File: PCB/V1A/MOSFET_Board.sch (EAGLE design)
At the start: 274 parts, among them IC301 78L05_TO-220AB-3-BR, IC302 78L05_TO-220AB-3-BR, J301 TEMP, J302 +12V, J303 CTRL, J304 FAN_MOLEX4PIN, J305 FAN_MOLEX4PIN, J306 DUT+, J307 DUT-, Q201 SIRC10DP, Q202 SIRC10DP, Q203 BC817, Q204 BC817, Q205 SIRC10DP, Q206 SIRC10DP, Q207 BC817, Q208 BC807, Q209 BC817, Q210 BC807, Q211 IXTK102N65X2, Q212 IXTK102N65X2, Q301 BC817, Q302 BC817, Q401 BC807, Q402 BC807, Q403 BC807, Q404 BC807, Q405 BC807, Q406 BC807, Q407 BC807, Q408 BC807, Q409 BC807, Q410 BC807, Q411 BC807, Q412 BC807, Q413 BC807, Q414 BC807, U201 AD420, U202 AD420, U203 LT1014I, U204 LT1014I, U205 AD620, U206 AD620, U207 AD620, U208 AD620, U209 LTC1865L, U210 LTC1865L, U301 LP2985-3.1, U302 LP2985-3.1, U303 LP2985-3.1, U304 AD620, U305 LTC1865L, U306 LTC1865L, U307 MAX743, U401 HCPL-063N, U402 HCPL-063N, U403 HCPL-063N, U404 HCPL-063N, U405 HCPL-063N, U406 HCPL-063N, U407 HCPL-063N

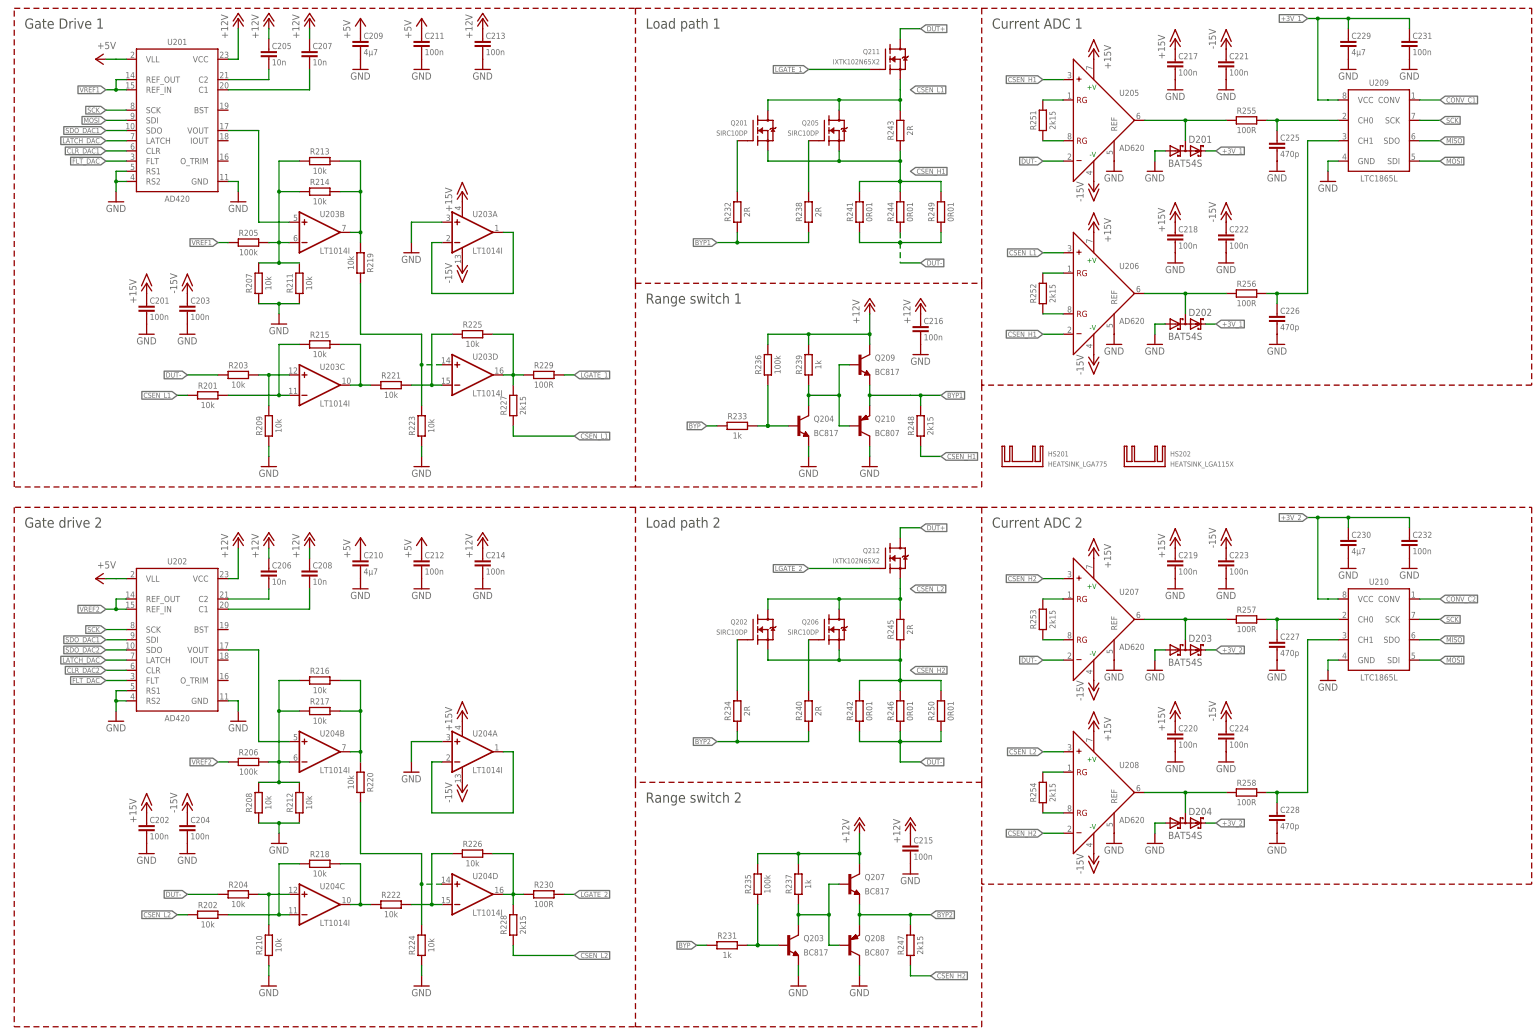
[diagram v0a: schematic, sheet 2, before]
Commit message: Added power amp for load MOSFET gate
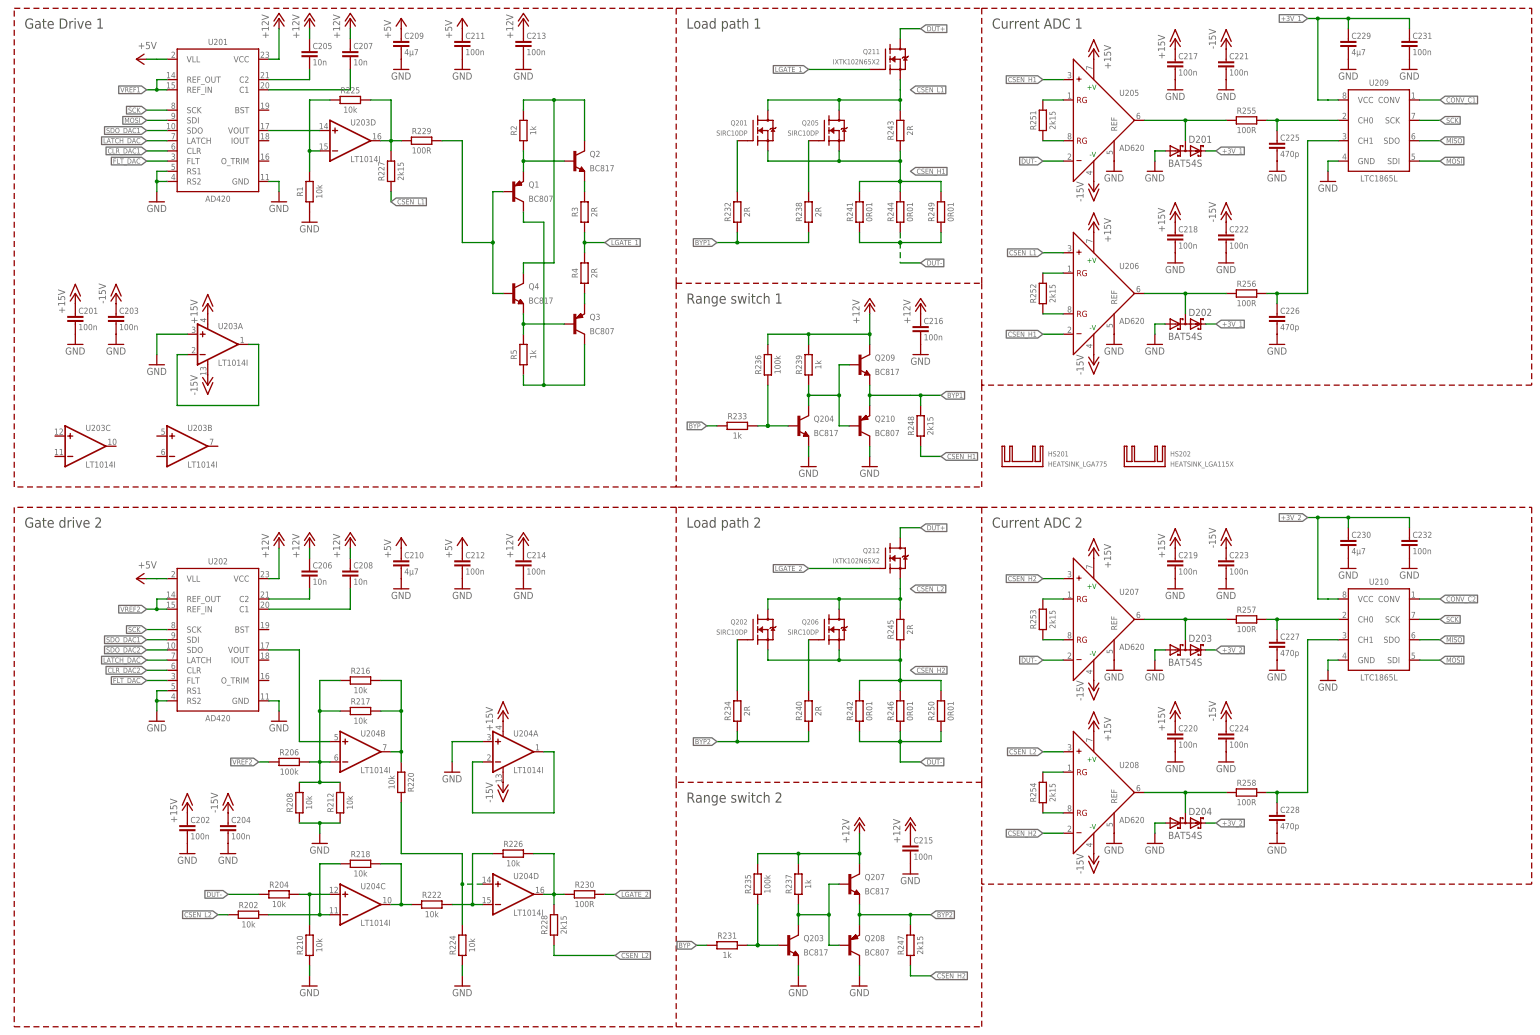
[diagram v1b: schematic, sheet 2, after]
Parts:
- removed R201, R203, R207, R209, R211, R213, R214, R215, R219, R221, R223: 10k, passives:R-EU-1608
- removed R205: 100k, passives:R-EU-1608
- added Q1, Q3: BC807, transistors:BC807
- added Q2, Q4: BC817, transistors:BC817
- added R1: 10k, passives:R-EU-1608
- added R2, R5: 1k, passives:R-EU-1608
- added R3, R4: 2R, passives:R-EU-3216
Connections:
- removed net N$12: R205.2, R207.2, R211.2, R213.1, R214.1, U203B.-IN
- new net N$67: Q1.B, Q4.B, R229.2
- new net N$68: Q3.B, Q4.E, R5.2
- net CSEN_L1: no longer R201.1
- net DAC_VOUT: now also U203D.+IN; no longer U203B.+IN
- net DUT-: no longer R203.1
- net GND: now also R1.1; no longer R207.1, R209.1, R211.1, R223.1
- net LGATE_1: now also R3.1, R4.2; no longer R229.2
- net N$1: now also Q1.E, Q2.B, R2.1; no longer R203.2, R209.2, U203C.+IN
- net N$11: now also Q3.E, R4.1; no longer R213.2, R214.2, R219.1, U203B.OUT
- net N$13: now also Q2.E, R3.2; no longer R215.2, R221.1, U203C.OUT
- net N$14: now also Q2.C, Q4.C, R2.2; no longer R201.2, R215.1, U203C.-IN
- net N$2: now also R1.2; no longer R221.2
- net N$9: now also Q1.C, Q3.C, R5.1; no longer R219.2, R223.2, U203D.+IN
- net VREF1: no longer R205.1
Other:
- moved on the sheet: C201, C202, C203, C204, C205, C206, C207, C208, C209, C210, C211, C212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

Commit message: Changed load path layout
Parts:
- removed C329, C340, C401, C402, C403, C404, C417, C418, C419: 100n, passives:C-EU-1608
- removed C330, C338, C339: 470n, passives:C-EU-1608
- removed C331: 10n, passives:C-EU-2012
- removed C332, C334, C335: 220µ, passives:CPOL_CAPPRD500W60D1000
- removed C333: 10µ, passives:CPOL-6032-C
- removed C337: 470p, passives:C-EU_CAPRR1000W80L1300T400H900
- removed C405, C406, C407, C408, C420, C421, C422: 10n, passives:C-EU-1608
- removed C409, C410, C411, C412, C413, C414, C415, C416, C423, C424, C425, C426, C427, C428: 15p, passives:C-EU-1608
- removed D204, D301: BAT54S, diode:BAT54S
- removed D302, D303: 1N5817-B, diode:1N5817-B
- removed HS201: HEATSINK_LGA775, mechanical:HEATSINK_LGA775
- removed HS202: HEATSINK_LGA115X, mechanical:HEATSINK_LGA115X
- removed IC301, IC302: 78L05_TO-220AB-3-BR, ic:78L05_TO-220AB-3-BR
- removed J301: TEMP, mechanical:HEAD_2X3_MALE
- removed J302: +12V, con-jack:JACK-PLUG1
- removed J303: CTRL, mechanical:HEAD_1X16_MALE
- removed J304, J305: FAN_MOLEX4PIN, mechanical:FAN_MOLEX4PIN
- removed J306: DUT+, mechanical:AMPHENOL_TERM-BLOCK_2
- removed J307: DUT-, mechanical:AMPHENOL_TERM-BLOCK_2
- removed L301, L302: 100µ, passives:L-EU_MSS1260
- removed L303: 4µ7, inductor-coilcraft:MSS7341
- removed MOV301, MOV302: 416NR10D, passives:MOV_9.5-DISK
- removed PS301: RFMM-0505S, modules:RFMM-0505S
- removed Q1, Q208, Q210, Q3, Q401, Q402, Q403, Q404, Q405, Q406, Q407, Q408, Q409, Q410, Q411, Q412, Q413, Q414: BC807, transistors:BC807
- removed Q2, Q203, Q204, Q207, Q209, Q4: BC817, transistors:BC817
- removed Q205, Q206: SIRC10DP, transistors:SIRC10DP
- removed Q211, Q212: IXTK102N65X2, transistors:IXTK102N65X2R
- removed R1, R216, R217, R218, R220, R222, R224, R225, R226: 10k, passives:R-EU-1608
- removed R2, R231, R233, R237, R239, R5: 1k, passives:R-EU-1608
- removed R227, R228, R247, R248, R251, R252, R253, R254: 2k15, passives:R-EU-2012
- removed R229, R230, R255, R256, R257, R258: 100R, passives:R-EU-1608
- removed R232, R234, R238, R240, R243, R245, R3, R4: 2R, passives:R-EU-3216
- removed R235, R236: 100k, passives:R-EU-1608
- removed R241, R242, R244, R246, R249, R250: 0R01, passives:R-EU-6332
- removed R401, R402, R403, R404, R405, R406, R407, R408, R409, R410, R411, R412, R413, R414, R415, R416, R417, R418, R419, R420, R421, R422, R423, R424, R425, R426, R427, R428: 350R, passives:R-EU-1608
- removed SJ301: DUT_GND, jumper:SJW
- removed U210: LTC1865L, ic:LTC1865L
- removed U401, U402, U403, U404, U405, U406, U407: HCPL-063N, ic:HCPL-063N
- added C101, C102, C133, C134: 4µ7, passives:C-EU-3216
- added C103, C104, C105, C106, C111, C112, C113, C114, C119, C120, C121, C122, C123, C124, C125, C126, C127, C128, C135, C136, C239: 100n, passives:C-EU-1608
- added C107, C108, C109, C110: 10n, passives:C-EU-2012
- added C115, C116, C117, C118, C237, C238: 470n, passives:C-EU-1608
- added C129, C130, C131, C132: 470p, passives:C-EU-1608
- added C233: 10µ, passives:CPOL-6032-C
- added C234, C235: 220µ, passives:CPOL_CAPPRD500W60D1000
- added C236: 470p, passives:C-EU_CAPRR1000W80L1300T400H900
- added D101, D102, D103, D104: BAT54S, diode:BAT54S
- added HS101: HEATSINK_LGA775, mechanical:HEATSINK_LGA775
- added HS102: HEATSINK_LGA115X, mechanical:HEATSINK_LGA115X
- added J201: TEMP, mechanical:HEAD_2X3_MALE
- added J202: +12V, con-jack:JACK-PLUG1
- added J203: CTRL, mechanical:HEAD_1X16_MALE
- added J204, J205: FAN_MOLEX4PIN, mechanical:FAN_MOLEX4PIN
- added J206: DUT+, mechanical:AMPHENOL_TERM-BLOCK_2
- added J207: DUT-, mechanical:AMPHENOL_TERM-BLOCK_2
- added L201, L202: 100µ, passives:L-EU_MSS1260
- added L203: 4µ7, inductor-coilcraft:MSS7341
- added MOV201, MOV202: 416NR10D, passives:MOV_9.5-DISK
- added PS201: RFMM-0505S, modules:RFMM-0505S
- added Q101, Q103, Q106, Q108, Q116, Q118, Q303, Q304, Q305, Q306, Q307, Q308, Q309, Q310, Q311, Q312, Q313, Q314: BC807, transistors:BC807
- added Q102, Q104, Q105, Q107, Q111, Q112, Q115, Q117: BC817, transistors:BC817
- added Q109, Q110, Q113, Q114: SIRC10DP, transistors:SIRC10DP
- added Q119, Q120: IXTK102N65X2, transistors:IXTK102N65X2R
- added R101, R102: 49k3, passives:R-EU-1608
- added R103, R104, R105, R106: 5k, passives:R-EU-1608
- added R107, R108, R109, R110, R112, R114, R118, R120, R123, R125: 2R, passives:R-EU-3216
- added R111, R113, R117, R119: 1k, passives:R-EU-1608
- added R115, R116: 100k, passives:R-EU-1608
- added R121, R122, R124, R126, R129, R130: 0R01, passives:R-EU-6332
- added R127, R128, R131, R132, R133, R134, R207: 2k15, passives:R-EU-2012
- added R135, R136, R137, R138, R209: 100R, passives:R-EU-1608
- added R201, R203, R205: 2M, passives:R-EU-3216
- added R211, R311, R314, R315, R316, R317, R318, R319, R320, R321, R322, R323, R324, R325, R326, R327, R328: 350R, passives:R-EU-1608
- added SJ201: DUT_GND, jumper:SJW
- added U101, U102: AD420, ic:AD420RW-24
- added U103, U104, U105, U106, U107, U108: AD620, ic:AD620R-8
- added U109, U110: LTC1865L, ic:LTC1865L
- C201, C202, C203, C217, C224: value 100n -> 4µ7; device passives:C-EU-1608 -> passives:C-EU-3216
- C208: value 10n -> 4µ7; device passives:C-EU-2012 -> passives:C-EU-3216
- C211, C212, C213, C215: value 100n -> 470n
- C218: value 100n -> 470p
- C223: value 100n -> 47µ; device passives:C-EU-1608 -> passives:CPOL-7343-DE
- C225: value 470p -> 4µ7; device passives:C-EU-1608 -> passives:C-EU-3216
- C226: value 470p -> 10n; device passives:C-EU-1608 -> passives:C-EU-2012
- C227: value 470p -> 10µ; device passives:C-EU-1608 -> passives:CPOL-6032-C
- C228, C318: value 470p -> 100n
- C229, C301, C302, C303, C317: value 4µ7 -> 100n; device passives:C-EU-3216 -> passives:C-EU-1608
- C230: value 4µ7 -> 470n; device passives:C-EU-3216 -> passives:C-EU-1608
- C231: value 100n -> 10n; device passives:C-EU-1608 -> passives:C-EU-2012
- C232: value 100n -> 220µ; device passives:C-EU-1608 -> passives:CPOL_CAPPRD500W60D1000
- C305, C306, C307: device passives:C-EU-2012 -> passives:C-EU-1608
- C308: value 4µ7 -> 10n; device passives:C-EU-3216 -> passives:C-EU-1608
- C309, C310, C324, C325: value 4µ7 -> 15p; device passives:C-EU-3216 -> passives:C-EU-1608
- C311, C312, C313, C315: value 470n -> 15p
- C314, C316, C328: value 100n -> 15p
- C320, C321, C322: value 100n -> 10n
- C323: value 47µ -> 15p; device passives:CPOL-7343-DE -> passives:C-EU-1608
- C326: value 10n -> 15p; device passives:C-EU-2012 -> passives:C-EU-1608
- C327: value 10µ -> 15p; device passives:CPOL-6032-C -> passives:C-EU-1608
- D202, D203: value BAT54S -> 1N5817-B; device diode:BAT54S -> diode:1N5817-B
- Q201, Q202: value SIRC10DP -> BC817; device transistors:SIRC10DP -> transistors:BC817
- Q301, Q302: value BC817 -> BC807; device transistors:BC817 -> transistors:BC807
- R202, R208: value 10k -> 2k15; device passives:R-EU-1608 -> passives:R-EU-2012
- R204: value 10k -> 2M; device passives:R-EU-1608 -> passives:R-EU-3216
- R206: value 100k -> 2M; device passives:R-EU-1608 -> passives:R-EU-3216
- R212, R310: value 10k -> 350R
- R301, R303, R304, R305, R306: value 2M -> 350R; device passives:R-EU-3216 -> passives:R-EU-1608
- R302, R307, R308: value 2k15 -> 350R; device passives:R-EU-2012 -> passives:R-EU-1608
- R309: value 100R -> 350R
- U201, U202: value AD420 -> LP2985-3.1; device ic:AD420RW-24 -> ic:LP2985-3.1
- U203: value LT1014I -> LP2985-3.1; device ic:LT1014ISW -> ic:LP2985-3.1
- U204: value LT1014I -> AD620; device ic:LT1014ISW -> ic:AD620R-8
- U205, U206: value AD620 -> 78L05_TO-220AB-3-BR; device ic:AD620R-8 -> ic:78L05_TO-220AB-3-BR
- U207, U208: value AD620 -> LTC1865L; device ic:AD620R-8 -> ic:LTC1865L
- U209: value LTC1865L -> MAX743; device ic:LTC1865L -> ic:MAX743WE
- U301, U302, U303: value LP2985-3.1 -> HCPL-063N; device ic:LP2985-3.1 -> ic:HCPL-063N
- U304: value AD620 -> HCPL-063N; device ic:AD620R-8 -> ic:HCPL-063N
- U305, U306: value LTC1865L -> HCPL-063N; device ic:LTC1865L -> ic:HCPL-063N
- U307: value MAX743 -> HCPL-063N; device ic:MAX743WE -> ic:HCPL-063N
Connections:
- removed net DAC_VOUT: U201.VOUT, U203D.+IN
- removed net DAC_VOUT1: U202.VOUT, U204B.+IN
- removed net N$52: R226.2, R228.2, R230.1, U204D.OUT
- removed net N$53: R220.2, R224.2, U204D.+IN
- removed net N$54: R216.2, R217.2, R220.1, U204B.OUT
- removed net N$55: U204A.-IN, U204A.OUT
- new net N$12: Q103.E, Q107.B, R105.1
- net +12V: now also C105.1, C106.1, C107.1, C108.1, C109.1, C110.1, C119.1, C120.1, C212.1, C232.+, J202.3, J204.+12V, J205.+12V, Q115.C, Q117.C, R115.2, R116.2, R117.2, R119.2, U101.VCC, U102.VCC, U205.VI, U206.VI; no longer C205.1, C206.1, C207.1, C208.1, C214.1, C215.1, C216.1, C312.1, C313.1, C332.+, IC301.VI, IC302.VI, J302.3, J304.+12V, J305.+12V, Q207.C, Q209.C, R235.2, R236.2, R237.2, R239.2, U201.VCC, U202.VCC
- net +15V: now also C111.1, C113.1, C115.1, C117.1, C121.1, C122.1, C123.1, C124.1, C216.1, Q102.C, Q104.C, Q105.C, Q107.C, Q202.E, R103.2, R105.2, U103.+V, U104.+V, U105.+V, U106.+V, U107.+V, U108.+V, U204.+V; no longer C201.1, C202.1, C217.1, C218.1, C219.1, C220.1, C316.1, Q302.E, U203A.V+, U204A.V+, U205.+V, U206.+V, U207.+V, U208.+V, U304.+V
- net +3V3: now also C210.1, R310.2, R311.2, R312.2, R314.2, R315.2, R316.2, R319.2, U203.VOUT; no longer C310.1, R410.2, R411.2, R412.2, R414.2, R415.2, R416.2, R419.2, U303.VOUT
- net +3V_1: now also C133.1, C135.1, C208.1, C217.1, C220.1, D101.C2, D102.C2, U109.VCC, U201.VOUT, U207.VCC; no longer C229.1, C231.1, C308.1, C317.1, C320.1, D201.C2, D202.C2, U209.VCC, U301.VOUT, U305.VCC
- net +3V_2: now also C134.1, C136.1, C209.1, C224.1, C228.1, D103.C2, D104.C2, D201.C2, U110.VCC, U202.VOUT, U208.VCC; no longer C230.1, C232.1, C309.1, C324.1, C328.1, D203.C2, D204.C2, D301.C2, U210.VCC, U302.VOUT, U306.VCC
- net +5V: now also C101.1, C102.1, C103.1, C104.1, C203.1, C204.1, C214.1, C221.1, C222.1, C223.+, C225.1, C229.2, C233.+, C301.1, C302.1, C305.1, C306.1, C307.1, C308.1, C317.1, C318.1, C320.1, J201.3, J201.4, L201.1, L203.2, R309.2, R313.2, R322.2, R323.2, R324.2, R326.2, R327.2, U101.VLL, U102.VLL, U203.ON/OFF, U203.VIN, U205.VO, U206.VO, U209.AV+, U209.V+, U209.V+@1, U209.V+@2, U209.V+@3, U301.VCC, U302.VCC, U303.VCC, U304.VCC, U305.VCC, U306.VCC; no longer C209.1, C210.1, C211.1, C212.1, C314.1, C322.1, C323.+, C325.1, C329.2, C333.+, C401.1, C402.1, C403.1, C404.1, C405.1, C406.1, C407.1, C408.1, C417.1, C418.1, C420.1, C421.1, IC301.VO, IC302.VO, J301.3, J301.4, L301.1, L303.2, R409.2, R413.2, R422.2, R423.2, R424.2, R426.2, R427.2, U201.VLL, U202.VLL, U303.ON/OFF, U303.VIN, U307.AV+, U307.V+, U307.V+@1, U307.V+@2, U307.V+@3, U401.VCC, U402.VCC, U403.VCC, U404.VCC, U405.VCC, U406.VCC
- net +5V_I: now also C236.2, C239.1, C319.1, C322.1, J203.16, PS201.+VO, R301.2, R302.2, R303.2, R304.2, R305.2, R306.2, R307.2, R308.2, R317.2, R318.2, R320.2, R321.2, R325.2, R328.2, U307.VCC; no longer C337.2, C340.1, C419.1, C422.1, J303.16, PS301.+VO, R401.2, R402.2, R403.2, R404.2, R405.2, R406.2, R407.2, R408.2, R417.2, R418.2, R420.2, R421.2, R425.2, R428.2, U407.VCC
- net -15V: now also C112.2, C114.2, C116.2, C118.2, C125.1, C126.1, C127.1, C128.1, C219.1, Q101.C, Q103.C, Q106.C, Q108.C, Q201.E, R104.1, R106.1, U103.-V, U104.-V, U105.-V, U106.-V, U107.-V, U108.-V, U204.-V; no longer C203.1, C204.1, C221.1, C222.1, C223.1, C224.1, C319.1, Q301.E, U203A.V-, U204A.V-, U205.-V, U206.-V, U207.-V, U208.-V, U304.-V
- net BPY1G1: now also Q109.G, R112.2; no longer Q201.G, R232.2
- net BYP: now also C309.1, R111.1, R113.1, R309.1, U301.VO1; no longer C409.1, R231.1, R233.1, R409.1, U401.VO1
- net BYP1: now also Q117.E, Q118.E, R112.1, R118.1, R128.1; no longer Q209.E, Q210.E, R232.1, R238.1, R248.1
- net BYP1G2: now also Q113.G, R118.2; no longer Q205.G, R238.2
- net BYP2: now also Q115.E, Q116.E, R114.1, R120.1, R127.2; no longer Q207.E, Q208.E, R234.1, R240.1, R247.2
- net BYP2G1: now also Q110.G, R114.2; no longer Q202.G, R234.2
- net BYP2G2: now also Q114.G, R120.2; no longer Q206.G, R240.2
- net BYP_I: now also J203.8, Q301.B; no longer J303.8, Q401.B
- net CLR_DAC1: now also C324.1, R324.1, U101.CLR, U306.VO1; no longer C424.1, R424.1, U201.CLR, U406.VO1
- net CLR_DAC1_I: now also J203.6, Q310.B; no longer J303.6, Q410.B
- net CLR_DAC2: now also C313.1, R313.1, U102.CLR, U301.VO2; no longer C413.1, R413.1, U202.CLR, U401.VO2
- net CLR_DAC2_I: now also J203.7, Q305.B; no longer J303.7, Q405.B
- net CONV_C1: now also C315.1, R315.1, U109.CONV, U303.VO2; no longer C415.1, R415.1, U209.CONV, U403.VO2
- net CONV_C1_I: now also J203.9, Q307.B; no longer J303.9, Q407.B
- net CONV_C2: now also C316.1, R316.1, U110.CONV, U304.VO2; no longer C416.1, R416.1, U210.CONV, U404.VO2
- net CONV_C2_I: now also J203.11, Q308.B; no longer J303.11, Q408.B
- net CONV_TEMP: now also C311.1, R311.1, U207.CONV, U303.VO1; no longer C411.1, R411.1, U305.CONV, U403.VO1
- net CONV_TEMP_I: now also J203.10, Q303.B; no longer J303.10, Q403.B
- net CONV_V: now also C312.1, R312.1, U208.CONV, U304.VO1; no longer C412.1, R412.1, U306.CONV, U404.VO1
- net CONV_V_I: now also J203.12, Q304.B; no longer J303.12, Q404.B
- net CSEN_H1: now also Q109.S, Q113.S, R121.2, R123.1, R124.2, R128.2, R129.2, U105.+, U106.-; no longer Q201.S, Q205.S, R241.2, R243.1, R244.2, R248.2, R249.2, U205.+, U206.-
- net CSEN_H2: now also Q110.S, Q114.S, R122.2, R125.1, R126.2, R127.1, R130.2, U107.+, U108.-; no longer Q202.S, Q206.S, R242.2, R245.1, R246.2, R247.1, R250.2, U207.+, U208.-
- net CSEN_L1: now also Q109.D, Q113.D, Q119.S, R123.2, U103.REF, U106.+; no longer Q201.D, Q205.D, Q211.S, R227.1, R243.2, U206.+
- net CSEN_L2: now also Q110.D, Q114.D, Q120.S, R125.2, U104.REF, U108.+; no longer Q202.D, Q206.D, Q212.S, R202.1, R228.1, R245.2, U208.+
- net DUT+: now also J206G$2.1, Q119.D, Q120.D; no longer J306G$2.1, Q211.D, Q212.D
- net DUT-: now also J207G$1.1, R121.1, R122.1, R124.1, R126.1, R129.1, R130.1, SJ201.2, U105.-, U107.-; no longer J307G$1.1, R204.1, R241.1, R242.1, R244.1, R246.1, R249.1, R250.1, SJ301.2, U205.-, U207.-
- net FAN1_PWM: now also C323.1, J204.PWM, R323.1, U305.VO1; no longer C423.1, J304.PWM, R423.1, U405.VO1
- net FAN1_PWM_I: now also J203.14, Q309.B; no longer J303.14, Q409.B
- net FAN1_SIG: now also J204.SIG; no longer J304.SIG
- net FAN2_PWM: now also C326.1, J205.PWM, R326.1, U305.VO2; no longer C426.1, J305.PWM, R426.1, U405.VO2
- net FAN2_PWM_I: now also J203.13, Q312.B; no longer J303.13, Q412.B
- net FAN2_SIG: now also J205.SIG; no longer J305.SIG
- net FLT_DAC: now also Q311.B, U101.FLT, U102.FLT; no longer Q411.B, U201.FLT, U202.FLT
- net FLT_DAC_I: now also C325.1, J203.1, R325.1, U307.VO1; no longer C425.1, J303.1, R425.1, U407.VO1
- net GND: now also C101.2, C102.2, C103.2, C104.2, C105.2, C106.2, C111.2, C112.1, C113.2, C114.1, C115.2, C116.1, C117.2, C118.1, C119.2, C120.2, C121.2, C122.2, C123.2, C124.2, C125.2, C126.2, C127.2, C128.2, C129.2, C130.2, C131.2, C132.2, C133.2, C134.2, C135.2, C136.2, C205.2, C206.2, C207.2, C208.2, C223.-, C226.1, C227.-, C229.1, C232.-, C233.-, C234.-, C235.+, C237.2, C238.2, C323.2, C326.2, C327.2, D101.A1, D102.A1, D103.A1, D104.A1, J201.1, J201.2, J202.1, J204.GND, J205.GND, L202.2, PS201.-VI, Q111.E, Q112.E, Q116.C, Q118.C, Q311.C, Q314.C, R207.1, SJ201.1, U101.GND, U101.RS1, U101.RS2, U102.GND, U102.RS1, U102.RS2, U103.-, U104.-, U105.REF, U106.REF, U107.REF, U108.REF, U109.GND, U110.GND, U203.GND, U204.REF, U205.GND, U206.GND, U207.GND, U208.GND, U209.12/15, U209.AGND, U304.GND, U307.C1, U307.C2; no longer C223.2, C226.2, C227.2, C229.2, C232.2, C319.2, C322.2, C323.-, C325.2, C326.1, C327.-, C328.2, C329.1, C330.2, C331.2, C332.-, C333.-, C334.-, C335.+, C338.2, C339.2, C401.2, C402.2, C403.2, C404.2, C405.2, C406.2, C407.2, C408.2, C409.2, C410.2, C411.2, C412.2, C413.2, C414.2, C415.2, C416.2, C417.2, C418.2, C420.2, C421.2, C423.2, C424.2, C426.2, C427.2, D202.A1, D203.A1, D204.A1, D301.A1, IC301.GND, IC302.GND, J301.1, J301.2, J302.1, J304.GND, J305.GND, L302.2, PS301.-VI, Q203.E, Q204.E, Q208.C, Q210.C, Q411.C, Q414.C, R1.1, R208.1, R212.1, R224.1, R307.1, R310.1, SJ301.1, U201.RS1, U201.RS2, U202.RS1, U202.RS2, U203A.+IN, U204A.+IN, U205.REF, U206.REF, U207.REF, U208.REF, U210.GND, U304.REF, U307.12/15, U307.AGND, U307.GND, U401.GND, U402.GND, U403.GND, U404.GND, U405.GND, U406.GND, U407.C1, U407.C2
- net GNDI: now also C239.2, C319.2, C322.2, C325.2, C328.2, J203.15, PS201.-VO, Q301.C, Q302.C, Q303.C, Q304.C, Q305.C, Q306.C, Q307.C, Q308.C, Q309.C, Q310.C, Q312.C, Q313.C, U301.C1, U301.C2, U302.C1, U302.C2, U303.C1, U303.C2, U304.C1, U304.C2, U305.C1, U305.C2, U306.C1, U306.C2, U307.GND; no longer C340.2, C419.2, C422.2, C425.2, C428.2, J303.15, PS301.-VO, Q401.C, Q402.C, Q403.C, Q404.C, Q405.C, Q406.C, Q407.C, Q408.C, Q409.C, Q410.C, Q412.C, Q413.C, U401.C1, U401.C2, U402.C1, U402.C2, U403.C1, U403.C2, U404.C1, U404.C2, U405.C1, U405.C2, U406.C1, U406.C2, U407.GND
- net HIGHC1: now also C129.1, R135.2, U109.CH0; no longer C225.1, R255.2, U209.CH0
- net HIGHC2: now also C131.1, R137.2, U110.CH0; no longer C227.1, R257.2, U210.CH0
- net LATCH_DAC: now also C327.1, R327.1, U101.LATCH, U102.LATCH, U306.VO2; no longer C427.1, R427.1, U201.LATCH, U202.LATCH, U406.VO2
- net LATCH_DAC_I: now also J203.5, Q313.B; no longer J303.5, Q413.B
- net LGATE_1: now also Q119.G, R107.1, R108.2; no longer Q211.G, R3.1, R4.2
- net LGATE_2: now also Q120.G, R109.1, R110.2; no longer Q212.G, R230.2
- net LOWC1: now also C130.1, R136.2, U109.CH1; no longer C226.1, R256.2, U209.CH1
- net LOWC2: now also C132.1, R138.2, U110.CH1; no longer C228.1, R258.2, U210.CH1
- net MISO: now also Q314.B, U109.SDO, U110.SDO, U207.SDO, U208.SDO; no longer Q414.B, U209.SDO, U210.SDO, U305.SDO, U306.SDO
- net MISO_I: now also C328.1, J203.2, R328.1, U307.VO2; no longer C428.1, J303.2, R428.1, U407.VO2
- net MOSI: now also C310.1, R310.1, U101.SDI, U109.SDI, U110.SDI, U207.SDI, U208.SDI, U302.VO1; no longer C410.1, R410.1, U201.SDI, U209.SDI, U210.SDI, U305.SDI, U306.SDI, U402.VO1
- net MOSI_I: now also J203.4, Q302.B; no longer J303.4, Q402.B
- net N$1: now also Q101.E, Q105.B, R103.1; no longer Q1.E, Q2.B, R2.1
- net N$10: now also C205.1, U201.BYP; no longer C305.1, U301.BYP
- net N$11: now also Q106.E, R108.1; no longer Q3.E, R4.1
- net N$13: now also Q105.E, R107.2; no longer Q2.E, R3.2
- net N$14: now also Q108.E, R110.1; no longer Q2.C, Q4.C, R2.2
- net N$15: now also Q107.E, R109.2; no longer U203A.-IN, U203A.OUT
- net N$16: now also D102.C1A2, R136.1, U106.OUT; no longer D202.C1A2, R256.1, U206.OUT
- net N$17: now also Q311.E, R319.1, U307.A1; no longer Q411.E, R419.1, U407.A1
- net N$18: now also Q314.E, R322.1, U307.A2; no longer Q414.E, R422.1, U407.A2
- net N$19: now also Q304.E, R304.1, U304.A1; no longer Q404.E, R404.1, U404.A1
- net N$2: now also R101.2, U103.RG@1; no longer R1.2, R225.1, U203D.-IN
- net N$20: now also Q308.E, R308.1, U304.A2; no longer Q408.E, R408.1, U404.A2
- net N$21: now also Q302.E, R302.1, U302.A1; no longer Q402.E, R402.1, U402.A1
- net N$22: now also Q306.E, R306.1, U302.A2; no longer Q406.E, R406.1, U402.A2
- net N$23: now also R209.1, U204.OUT; no longer R309.1, U304.OUT
- net N$24: now also R205.1, R206.2; no longer R305.1, R306.2
- net N$25: now also Q111.C, Q115.B, Q116.B, R117.1; no longer Q203.C, Q207.B, Q208.B, R237.1
- net N$26: now also R203.2, R205.2; no longer R303.2, R305.2
- net N$27: now also R203.1, R204.2; no longer R303.1, R304.2
- net N$28: now also MOV201.2, MOV202.1; no longer MOV301.2, MOV302.1
- net N$29: now also R206.1, R207.2, U204.+; no longer R306.1, R307.2, U304.+
- net N$3: now also C107.2, U101.C2; no longer C205.2, U201.C2
- net N$30: now also C218.1, D201.C1A2, R209.2, U208.CH0; no longer C318.1, D301.C1A2, R309.2, U306.CH0
- net N$31: now also Q111.B, R111.2, R115.1; no longer Q203.B, R231.2, R235.1
- net N$32: now also C234.+, D202.C, Q202.C, R211.1, U209.FB+; no longer C334.+, D302.C, Q302.C, R312.1, U307.FB+
- net N$33: now also R201.2, R204.1; no longer R301.2, R304.1
- net N$34: now also C231.1, U209.CC-; no longer C331.1, U307.CC-
- net N$35: now also C230.1, U209.SS; no longer C330.1, U307.SS
- net N$36: now also R202.2, U204.-; no longer R302.2, U304.-
- net N$37: now also C226.2, U209.CC+; no longer C326.2, U307.CC+
- net N$38: now also D202.A, L201.2, U209.LX+; no longer D302.A, L301.2, U307.LX+
- net N$39: now also D203.C, L202.1, U209.LX-; no longer D303.C, L302.1, U307.LX-
- net N$4: now also C109.2, U101.C1; no longer C207.2, U201.C1
- net N$40: now also Q309.E, R317.1, U305.A1; no longer Q409.E, R417.1, U405.A1
- net N$41: now also C108.2, U102.C2; no longer C206.2, U202.C2
- net N$42: now also C110.2, U102.C1; no longer C208.2, U202.C1
- net N$43: now also Q103.B, Q104.B, U104.OUT; no longer R206.2, R208.2, R212.2, R216.1, R217.1, U204B.-IN
- net N$44: now also Q104.E, Q108.B, R106.2; no longer R218.2, R222.1, U204C.OUT
- net N$45: now also R210.2, U208.CH1; no longer R310.2, U306.CH1
- net N$46: now also Q312.E, R320.1, U305.A2; no longer Q412.E, R420.1, U405.A2
- net N$47: now also Q301.E, R301.1, U301.A1; no longer Q401.E, R401.1, U401.A1
- net N$48: now also Q305.E, R305.1, U301.A2; no longer Q405.E, R405.1, U401.A2
- net N$49: now also R102.2, U104.RG@1; no longer R202.2, R218.1, U204C.-IN
- net N$5: now also Q112.C, Q117.B, Q118.B, R119.1; no longer Q204.C, Q209.B, Q210.B, R239.1
- net N$50: now also R102.1, U104.RG@2; no longer R204.2, R210.2, U204C.+IN
- net N$51: now also U102.VOUT, U104.+; no longer R222.2, R226.1, U204D.-IN
- net N$56: now also D103.C1A2, R137.1, U107.OUT; no longer D203.C1A2, R257.1, U207.OUT
- net N$57: now also D104.C1A2, R138.1, U108.OUT; no longer D204.C1A2, R258.1, U208.OUT
- net N$58: now also Q310.E, R318.1, U306.A1; no longer Q410.E, R418.1, U406.A1
- net N$59: now also Q313.E, R321.1, U306.A2; no longer Q413.E, R421.1, U406.A2
- net N$6: now also R101.1, U103.RG@2; no longer R225.2, R227.2, R229.1, U203D.OUT
- net N$60: now also C236.1, L203.1, PS201.+VI; no longer C337.1, L303.1, PS301.+VI
- net N$62: now also C206.1, U202.BYP; no longer C306.1, U302.BYP
- net N$63: now also C238.1, Q202.B, R211.2; no longer C339.1, Q302.B, R312.2
- net N$64: now also C235.-, D203.A, Q201.C, R212.1, U209.FB-; no longer C335.-, D303.A, Q301.C, R313.1, U307.FB-
- net N$65: now also C237.1, Q201.B, R212.2; no longer C338.1, Q301.B, R313.2
- net N$66: now also C207.1, U203.BYP; no longer C307.1, U303.BYP
- net N$67: now also Q101.B, Q102.B, U103.OUT; no longer Q1.B, Q4.B, R229.2
- net N$68: now also Q102.E, Q106.B, R104.2; no longer Q3.B, Q4.E, R5.2
- net N$7: now also D101.C1A2, R135.1, U105.OUT; no longer D201.C1A2, R255.1, U205.OUT
- net N$76: now also Q303.E, R303.1, U303.A1; no longer Q403.E, R403.1, U403.A1
- net N$77: now also Q307.E, R307.1, U303.A2; no longer Q407.E, R407.1, U403.A2
- net N$8: now also Q112.B, R113.2, R116.1; no longer Q204.B, R233.2, R236.1
- net N$9: now also U101.VOUT, U103.+; no longer Q1.C, Q3.C, R5.1
- net RG1_H6: now also R208.2, U204.RG@1; no longer R308.2, U304.RG@1
- net RG1_L1: now also R133.2, U107.RG@1; no longer R253.2, U207.RG@1
- net RG1_L2: now also R134.2, U108.RG@1; no longer R254.2, U208.RG@1
- net RG1_L3: now also R131.2, U105.RG@1; no longer R251.2, U205.RG@1
- net RG1_L4: now also R132.2, U106.RG@1; no longer R252.2, U206.RG@1
- net RG2_H6: now also R208.1, U204.RG@2; no longer R308.1, U304.RG@2
- net RG2_L1: now also R133.1, U107.RG@2; no longer R253.1, U207.RG@2
- net RG2_L2: now also R134.1, U108.RG@2; no longer R254.1, U208.RG@2
- net RG2_L3: now also R131.1, U105.RG@2; no longer R251.1, U205.RG@2
- net RG2_L4: now also R132.1, U106.RG@2; no longer R252.1, U206.RG@2
- net SCK: now also C314.1, R314.1, U101.SCK, U102.SCK, U109.SCK, U110.SCK, U207.SCK, U208.SCK, U302.VO2; no longer C414.1, R414.1, U201.SCK, U202.SCK, U209.SCK, U210.SCK, U305.SCK, U306.SCK, U402.VO2
- net SCK_I: now also J203.3, Q306.B; no longer J303.3, Q406.B
- net SDO_DAC1: now also U101.SDO, U102.SDI; no longer U201.SDO, U202.SDI
- net SDO_DAC2: now also U102.SDO; no longer U202.SDO
- net TEMP1: now also C211.1, J201.5, U207.CH0; no longer C311.1, J301.5, U305.CH0
- net TEMP2: now also C215.1, J201.6, U207.CH1; no longer C315.1, J301.6, U305.CH1
- net VREF1: now also C201.1, U101.REF_IN, U101.REF_OUT, U201.ON/OFF, U201.VIN; no longer C301.1, U201.REF_IN, U201.REF_OUT, U301.ON/OFF, U301.VIN
- net VREF2: now also C202.1, U102.REF_IN, U102.REF_OUT, U202.ON/OFF, U202.VIN; no longer C302.1, R206.1, U202.REF_IN, U202.REF_OUT, U302.ON/OFF, U302.VIN
- net VREF_MAX743: now also C227.+, U209.VREF; no longer C327.+, U307.VREF
- net VSENSE+: now also J206G$1.1, MOV201.1, R201.1; no longer J306G$1.1, MOV301.1, R301.1
- net VSENSE-: now also J207G$2.1, MOV202.2, R202.1; no longer J307G$2.1, MOV302.2, R302.1
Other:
- note removed: "+12V"
- note removed: "+12VDC"
- note removed: "+15V"
- note removed: "+15VDC"
- note removed: "+3VDC"
- note removed: "+5V"
- note removed: "+5VDC"
- note removed: "-15V"
- note removed: "-15VDC"
- note removed: "0R002"
- note removed: "2R"
- note removed: "5VDC<-5VDC"
- note removed: "7805"
- note removed: "DAC"
- note removed: "DUT"
- note removed: "Gate Drive"
- note removed: "I/O"
- note removed: "LDO"
- note removed: "MAX743"
- note removed: "MOSFET"
- note removed: "Optocouplers"
- note removed: "Range Switch"
- note removed: "TODO: block diagram"
- note removed: "Vout"
- note removed: "Vref"

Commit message: Cleaned up schematic; PCB layout
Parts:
- added R1: 1k, passives:R-EU-1608
- R310, R311, R312, R314, R315, R316: value 350R -> 1k
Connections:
- net +3V3: no longer R319.2
- net +5V: now also R1.2, R319.2
- net GND: no longer R207.1
- net MISO: now also R1.1
- net VSENSE-: now also R207.1
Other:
- note removed: "Current ADC 1"
- note removed: "Load path 1"
- note removed: "Range switch 1"
- moved on the sheet: C115, C116, C120, C121, C122, C125, C126, C129, C130, C133, C135, D101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

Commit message: Schematic layout
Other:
- note removed: "Current ADC 2"
- note removed: "Load path 2"
- note removed: "Range switch 2"
- moved on the sheet: C102, C104, C106, C108, C110, C113, C114, C117, C118, C119, C123, C124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

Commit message: PCB layout
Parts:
- removed C213: 470n, passives:C-EU-1608
- removed C222, C239: 100n, passives:C-EU-1608
- removed C233: 10µ, passives:CPOL-6032-C
- removed C236: 470p, passives:C-EU_CAPRR1000W80L1300T400H900
- removed L203: 4µ7, inductor-coilcraft:MSS7341
- removed PS201: RFMM-0505S, modules:RFMM-0505S
- removed U206: 78L05_TO-220AB-3-BR, ic:78L05_TO-220AB-3-BR
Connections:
- removed net N$60: C236.1, L203.1, PS201.+VI
- net +12V: no longer C213.1, U206.VI
- net +5V: no longer C222.1, C233.+, L203.2, U206.VO
- net +5V_I: no longer C236.2, C239.1, PS201.+VO
- net GND: no longer C213.2, C222.2, C233.-, PS201.-VI, U206.GND
- net GNDI: no longer C239.2, PS201.-VO
